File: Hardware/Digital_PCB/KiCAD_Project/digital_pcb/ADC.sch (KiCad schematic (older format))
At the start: 18 parts, among them U4 ADS1220, U5 KC2520B-C2

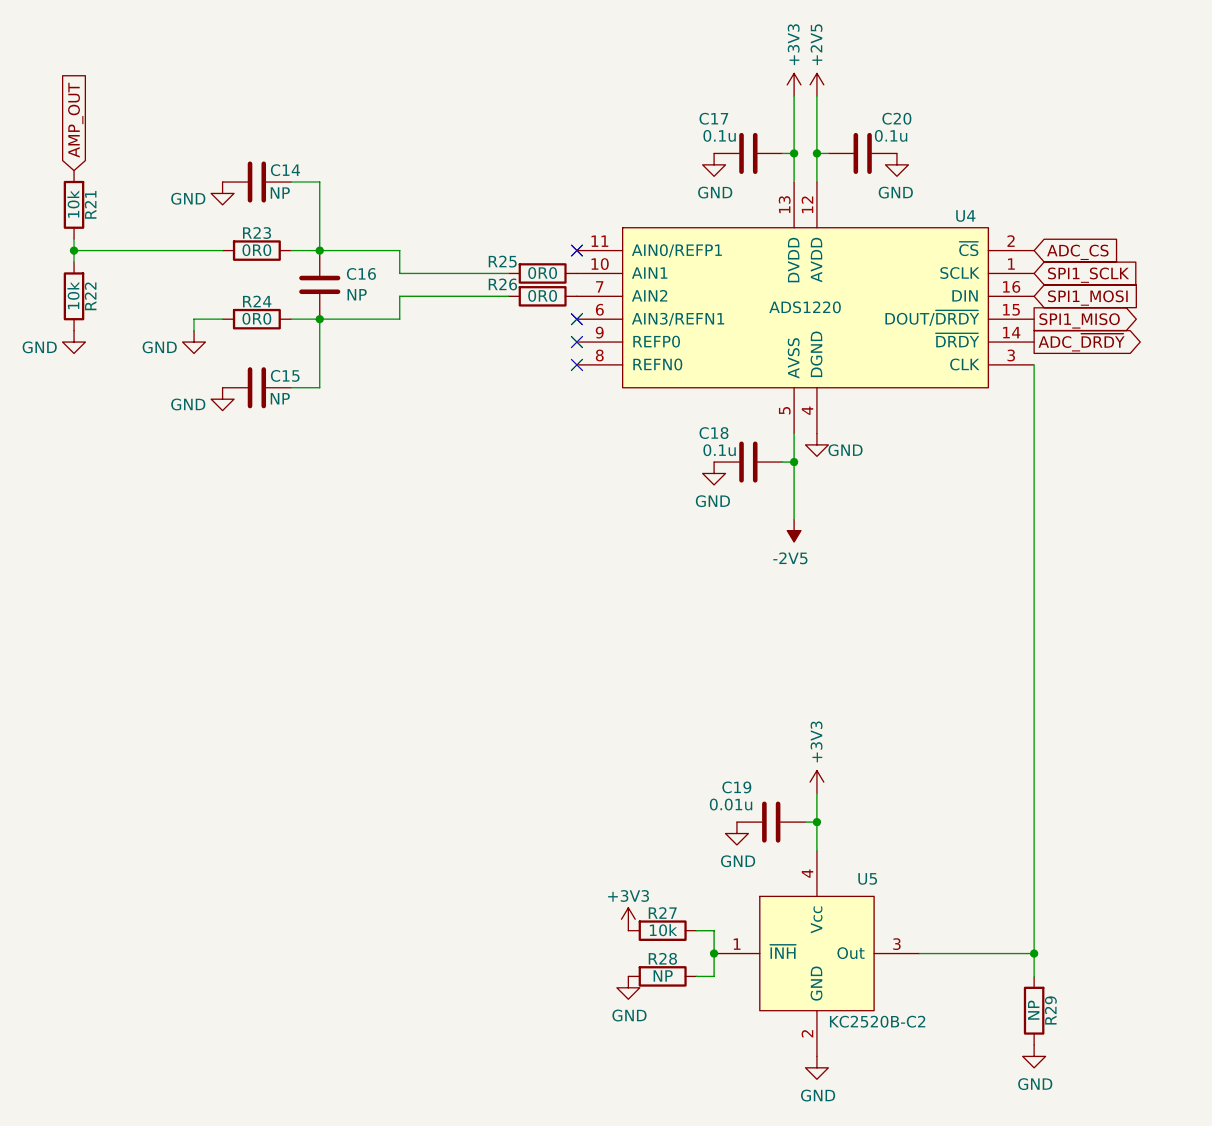
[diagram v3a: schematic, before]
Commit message: Update footprints
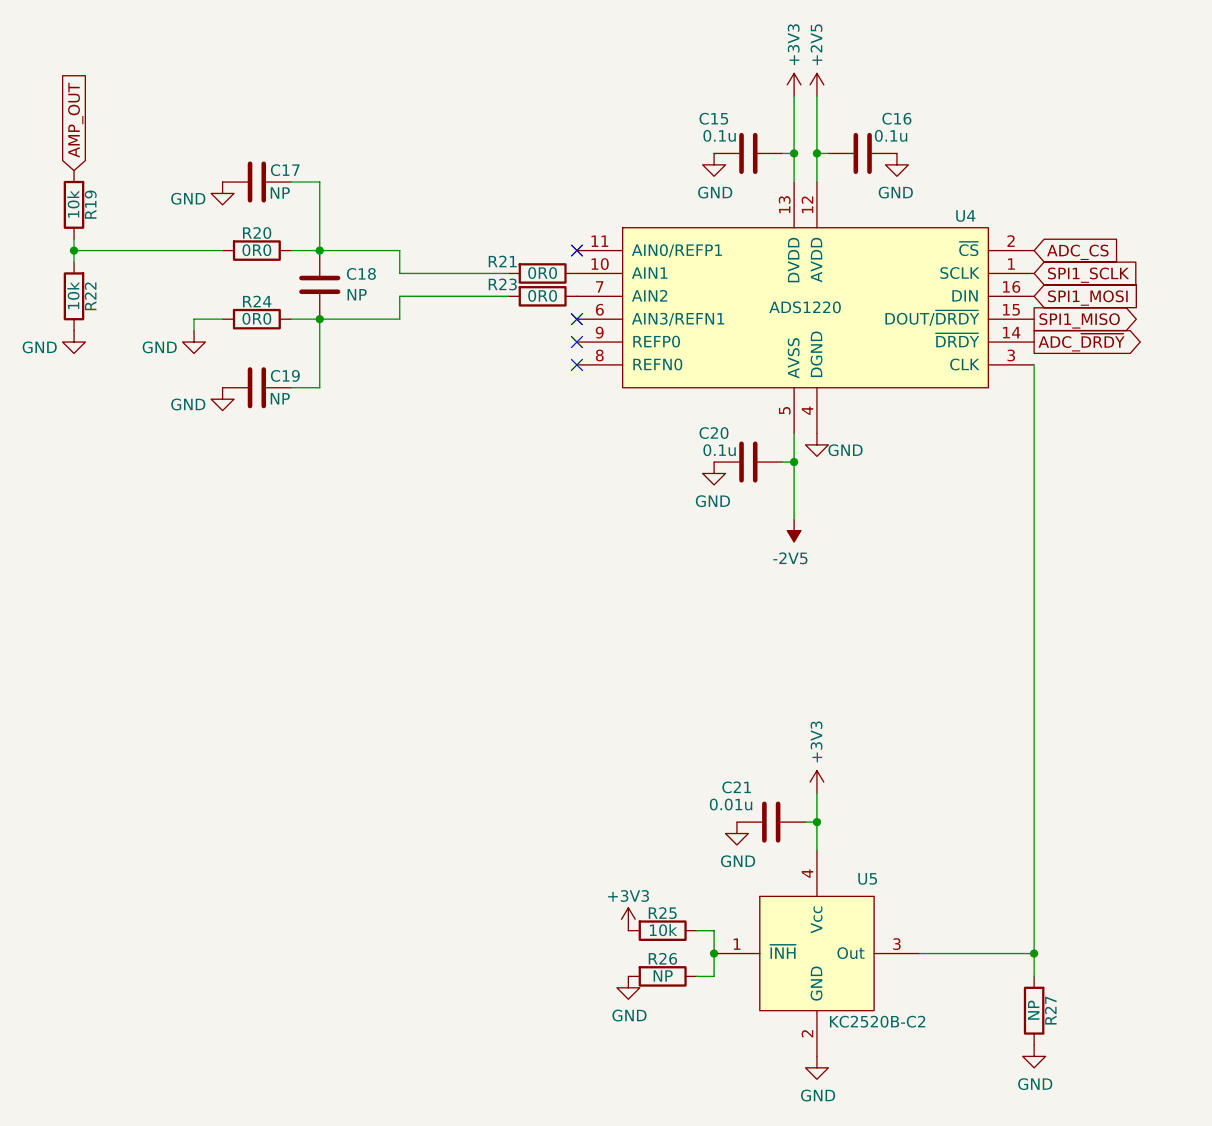
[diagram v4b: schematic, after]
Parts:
- C15: renamed from C17; footprint Capacitors_SMD:C_0603_HandSoldering -> Capacitor_SMD:C_0603_1608Metric
- C16: renamed from C20; footprint Capacitors_SMD:C_0603_HandSoldering -> Capacitor_SMD:C_0603_1608Metric
- C17: renamed from C14; footprint Capacitors_SMD:C_0603_HandSoldering -> Capacitor_SMD:C_0603_1608Metric
- C18: renamed from C16; footprint Capacitors_SMD:C_0603_HandSoldering -> Capacitor_SMD:C_0603_1608Metric
- C19: renamed from C15; footprint Capacitors_SMD:C_0603_HandSoldering -> Capacitor_SMD:C_0603_1608Metric
- C20: renamed from C18; footprint Capacitors_SMD:C_0603_HandSoldering -> Capacitor_SMD:C_0603_1608Metric
- C21: renamed from C19; footprint Capacitors_SMD:C_0603_HandSoldering -> Capacitor_SMD:C_0603_1608Metric
- R19: renamed from R21; footprint Resistors_SMD:R_0603_HandSoldering -> Resistor_SMD:R_0603_1608Metric
- R20: renamed from R23; footprint Resistors_SMD:R_0603_HandSoldering -> Resistor_SMD:R_0603_1608Metric
- R21: renamed from R25; footprint Resistors_SMD:R_0603_HandSoldering -> Resistor_SMD:R_0603_1608Metric
- R22, R24: footprint Resistors_SMD:R_0603_HandSoldering -> Resistor_SMD:R_0603_1608Metric
- R23: renamed from R26; footprint Resistors_SMD:R_0603_HandSoldering -> Resistor_SMD:R_0603_1608Metric
- R25: renamed from R27; footprint Resistors_SMD:R_0603_HandSoldering -> Resistor_SMD:R_0603_1608Metric
- R26: renamed from R28; footprint Resistors_SMD:R_0603_HandSoldering -> Resistor_SMD:R_0603_1608Metric
- R27: renamed from R29; footprint Resistors_SMD:R_0603_HandSoldering -> Resistor_SMD:R_0603_1608Metric
